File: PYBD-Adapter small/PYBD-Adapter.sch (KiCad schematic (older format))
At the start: 5 parts, among them J1 Conn_01x16, J2 Conn_01x16, J3 Conn_01x16, J4 Conn_01x16

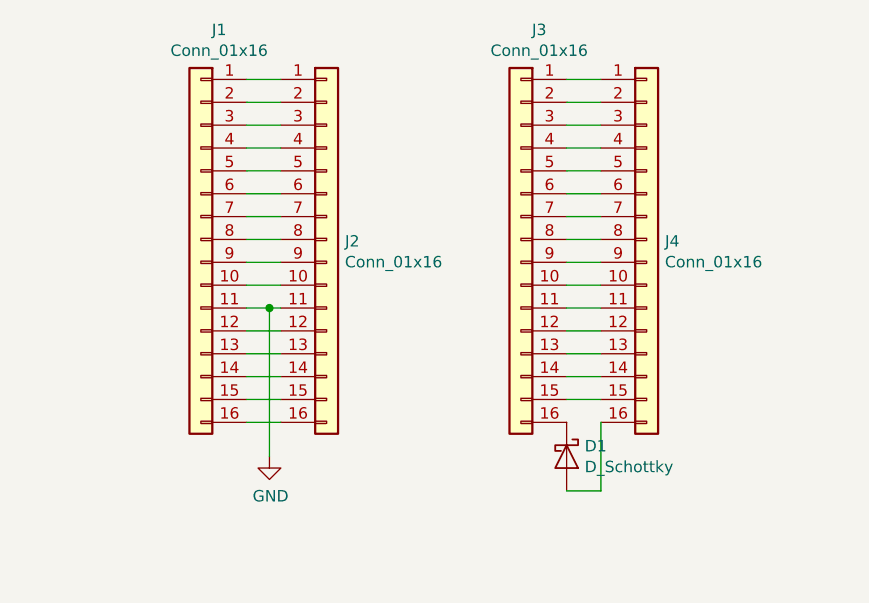
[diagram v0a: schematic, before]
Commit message: Small Adapter: Add switches for reset and boot
Change diode pad to hold SMD parts.
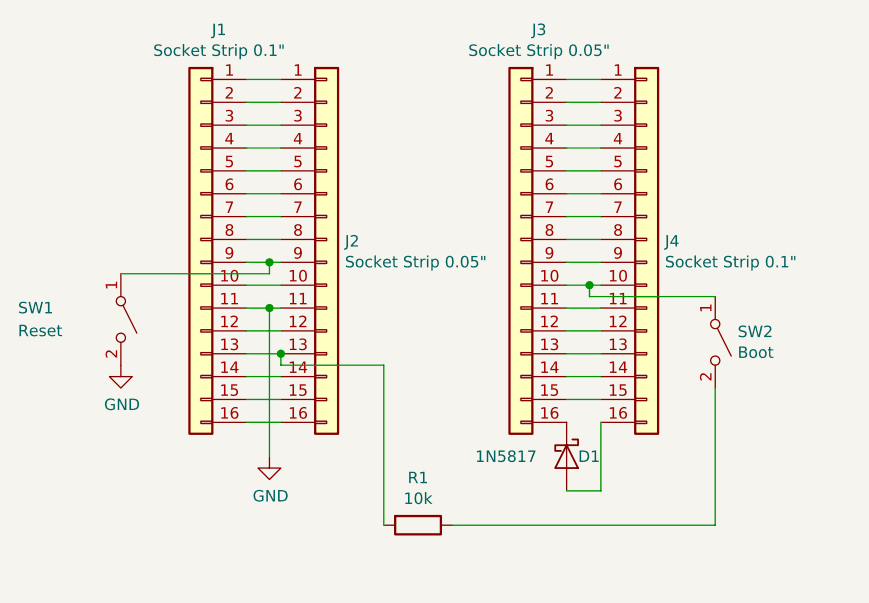
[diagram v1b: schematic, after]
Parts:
- added R1: 10k, Resistor_SMD:R_1206_3216Metric_Pad1.42x1.75mm_HandSolder, symbol Device:R
- added SW1: Reset, Button_Switch_SMD:Panasonic_EVQPUJ_EVQPUA, symbol Switch:SW_SPST
- added SW2: Boot, Button_Switch_SMD:Panasonic_EVQPUJ_EVQPUA, symbol Switch:SW_SPST
- D1: value D_Schottky -> 1N5817; footprint Diode_THT:D_DO-41_SOD81_P7.62mm_Horizontal -> Diode_SMD:D_SMB_Handsoldering
- J1, J4: value Conn_01x16 -> Socket Strip 0.1\"
- J2, J3: value Conn_01x16 -> Socket Strip 0.05\"
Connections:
- net GND: now also SW1.2 (B)
- net at J1.13 (Pin_13), J2.13 (Pin_13): now also R1.2
- net at J1.9 (Pin_9), J2.9 (Pin_9): now also SW1.1 (A)
- net at J3.10 (Pin_10), J4.10 (Pin_10): now also SW2.1 (A)
- new net: R1.1, SW2.2 (B)
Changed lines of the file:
@@
 P 6950 3150
 F 0 "J2" H 7030 3142 50  0000 L CNN
-F 1 "Conn_01x16" H 7030 3051 50  0000 L CNN
+F 1 "Socket Strip 0.05\"" H 7030 3051 50  0000 L CNN
 F 2 "Connector_PinSocket_1.27mm:PinSocket_1x16_P1.27mm_Vertical" H 6950 3150 50  0001 C CNN
 F 3 "~" H 6950 3150 50  0001 C CNN
@@
 P 6400 3150
 F 0 "J1" H 6320 4067 50  0000 C CNN
-F 1 "Conn_01x16" H 6320 3976 50  0000 C CNN
+F 1 "Socket Strip 0.1\"" H 6320 3976 50  0000 C CNN
 F 2 "Connector_PinSocket_2.54mm:PinSocket_2x08_P2.54mm_Vertical" H 6400 3150 50  0001 C CNN
 F 3 "~" H 6400 3150 50  0001 C CNN
@@
 P 8350 3150
 F 0 "J4" H 8430 3142 50  0000 L CNN
-F 1 "Conn_01x16" H 8430 3051 50  0000 L CNN
+F 1 "Socket Strip 0.1\"" H 8430 3051 50  0000 L CNN
 F 2 "Connector_PinSocket_2.54mm:PinSocket_2x08_P2.54mm_Vertical" H 8350 3150 50  0001 C CNN
 F 3 "~" H 8350 3150 50  0001 C CNN
@@
 P 7800 3150
 F 0 "J3" H 7720 4067 50  0000 C CNN
-F 1 "Conn_01x16" H 7720 3976 50  0000 C CNN
+F 1 "Socket Strip 0.05\"" H 7720 3976 50  0000 C CNN
 F 2 "Connector_PinSocket_1.27mm:PinSocket_1x16_P1.27mm_Vertical" H 7800 3150 50  0001 C CNN
 F 3 "~" H 7800 3150 50  0001 C CNN
@@
 	6600 3150 6750 3150
 Wire Wire Line
-	6600 3250 6750 3250
+	6600 3250 6700 3250
 Wire Wire Line
 	6600 3350 6750 3350
@@
 	8000 3250 8150 3250
 Wire Wire Line
-	8000 3350 8150 3350
+	8000 3350 8100 3350
 Wire Wire Line
 	8000 3450 8150 3450
@@
 U 1 1 5D01EE87
 P 8000 4100
-F 0 "D1" V 7954 4179 50  0000 L CNN
-F 1 "D_Schottky" V 8045 4179 50  0000 L CNN
-F 2 "Diode_THT:D_DO-41_SOD81_P7.62mm_Horizontal" H 8000 4100 50  0001 C CNN
+F 0 "D1" V 8000 4150 50  0000 L CNN
+F 1 "1N5817" V 8000 3700 50  0000 L CNN
+F 2 "Diode_SMD:D_SMB_Handsoldering" H 8000 4100 50  0001 C CNN
 F 3 "~" H 8000 4100 50  0001 C CNN
 	1    8000 4100
@@
 Wire Wire Line
 	8150 4250 8150 3950
+$Comp
+L Switch:SW_SPST SW1
+U 1 1 5DA4CB73
+P 6050 3500
+F 0 "SW1" V 6000 3050 50  0000 L CNN
+F 1 "Reset" V 6100 3050 50  0000 L CNN
+F 2 "Button_Switch_SMD:Panasonic_EVQPUJ_EVQPUA" H 6050 3500 50  0001 C CNN
+F 3 "" H 6050 3500 50  0001 C CNN
+	1    6050 3500
+	0    1    1    0
+$EndComp
+Wire Wire Line
+	6050 3300 6700 3300
+Wire Wire Line
+	6700 3300 6700 3250
+Connection ~ 6700 3250
+Wire Wire Line
+	6700 3250 6750 3250
+$Comp
+L power:GND #PWR0102
+U 1 1 5DA4DA3B
+P 6050 3700
+F 0 "#PWR0102" H 6050 3450 50  0001 C CNN
+F 1 "GND" H 6055 3527 50  0000 C CNN
+F 2 "" H 6050 3700 50  0001 C CNN
+F 3 "" H 6050 3700 50  0001 C CNN
+	1    6050 3700
+	1    0    0    -1
+$EndComp
+$Comp
+L Switch:SW_SPST SW2
+U 1 1 5DA4DB93
+P 8650 3600
+F 0 "SW2" V 8604 3698 50  0000 L CNN
+F 1 "Boot" V 8695 3698 50  0000 L CNN
+F 2 "Button_Switch_SMD:Panasonic_EVQPUJ_EVQPUA" H 8650 3600 50  0001 C CNN
+F 3 "" H 8650 3600 50  0001 C CNN
+	1    8650 3600
+	0    1    1    0
+$EndComp
+Wire Wire Line
+	8100 3350 8100 3400
+Wire Wire Line
+	8100 3400 8650 3400
+Connection ~ 8100 3350
+Wire Wire Line
+	8100 3350 8150 3350
+Wire Wire Line
+	7200 4400 7200 3700
+Wire Wire Line
+	7200 3700 6750 3700
+Wire Wire Line
+	6750 3700 6750 3650
+Connection ~ 6750 3650
+$Comp
+L Device:R R1
+U 1 1 5DA71EA6
+P 7350 4400
+F 0 "R1" V 7143 4400 50  0000 C CNN
+F 1 "10k" V 7234 4400 50  0000 C CNN
+F 2 "Resistor_SMD:R_1206_3216Metric_Pad1.42x1.75mm_HandSolder" V 7280 4400 50  0001 C CNN
+F 3 "~" H 7350 4400 50  0001 C CNN
+	1    7350 4400
+	0    1    1    0
+$EndComp
+Wire Wire Line
+	7500 4400 8650 4400
+Wire Wire Line
+	8650 3800 8650 4400
 $EndSCHEMATC

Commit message: Small Adapter: Add mounting holes for the switch
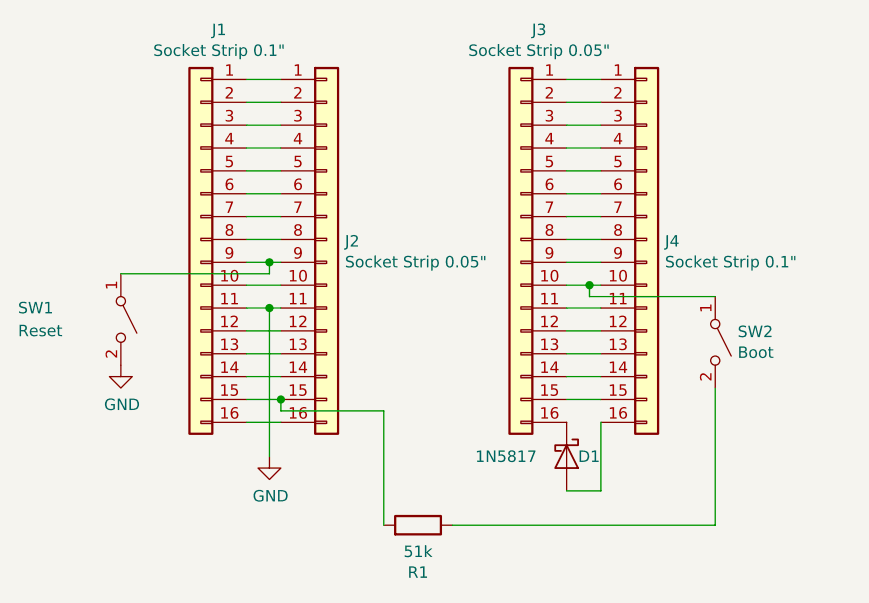
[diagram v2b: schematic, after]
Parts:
- R1: value 10k -> 51k
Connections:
- net at J1.13 (Pin_13), J2.13 (Pin_13): no longer R1.2
- net at J1.15 (Pin_15), J2.15 (Pin_15): now also R1.2
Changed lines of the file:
@@
 Wire Wire Line
 	8100 3350 8150 3350
-Wire Wire Line
-	7200 4400 7200 3700
-Wire Wire Line
-	7200 3700 6750 3700
-Wire Wire Line
-	6750 3700 6750 3650
-Connection ~ 6750 3650
 $Comp
 L Device:R R1
@@
 P 7350 4400
 F 0 "R1" V 7143 4400 50  0000 C CNN
-F 1 "10k" V 7234 4400 50  0000 C CNN
+F 1 "51k" V 7234 4400 50  0000 C CNN
 F 2 "Resistor_SMD:R_1206_3216Metric_Pad1.42x1.75mm_HandSolder" V 7280 4400 50  0001 C CNN
 F 3 "~" H 7350 4400 50  0001 C CNN
 	1    7350 4400
-	0    1    1    0
+	0    1    -1   0
 $EndComp
 Wire Wire Line
@@
 Wire Wire Line
 	8650 3800 8650 4400
+Wire Wire Line
+	7200 4400 7200 3900
+Wire Wire Line
+	7200 3900 6750 3900
+Wire Wire Line
+	6750 3900 6750 3850
+Connection ~ 6750 3850
 $EndSCHEMATC
